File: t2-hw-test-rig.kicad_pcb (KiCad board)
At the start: 2 copper layers, 86.4 x 94 mm, 152 parts, among them J101 CONN_01X02, J102 BARREL_JACK, J103 CONN_01X02, J201 MICROUSB-TH, J202 CONN_01X02, J203 MICROUSB-TH, J204 USB_A_TH, J301 CONN_02x05, 0.05", Q101 pMOS, Q401 CJ2302, Q402 CJ2302, Q403 CJ2302, Q404 CJ2302, Q405 CJ2302 DNP, Q406 CJ2302 DNP, SW301 Switch_DPST, SW302 Switch_DPST, U101 MAX6102, U102 XC6206P332MR-G, U301 ATSAMD21J18A-MUT, U302 AAT4610, U303 AAT4610, U401 MAX9919FASA+, U402 MAX9919FASA+, U403 MAX9919FASA+, U404 MAX9919FASA+, U405 MAX9919FASA+, U501 TSV324IDT, U502 TSV324IDT, U503 TSV324IDT, X301 FC-135

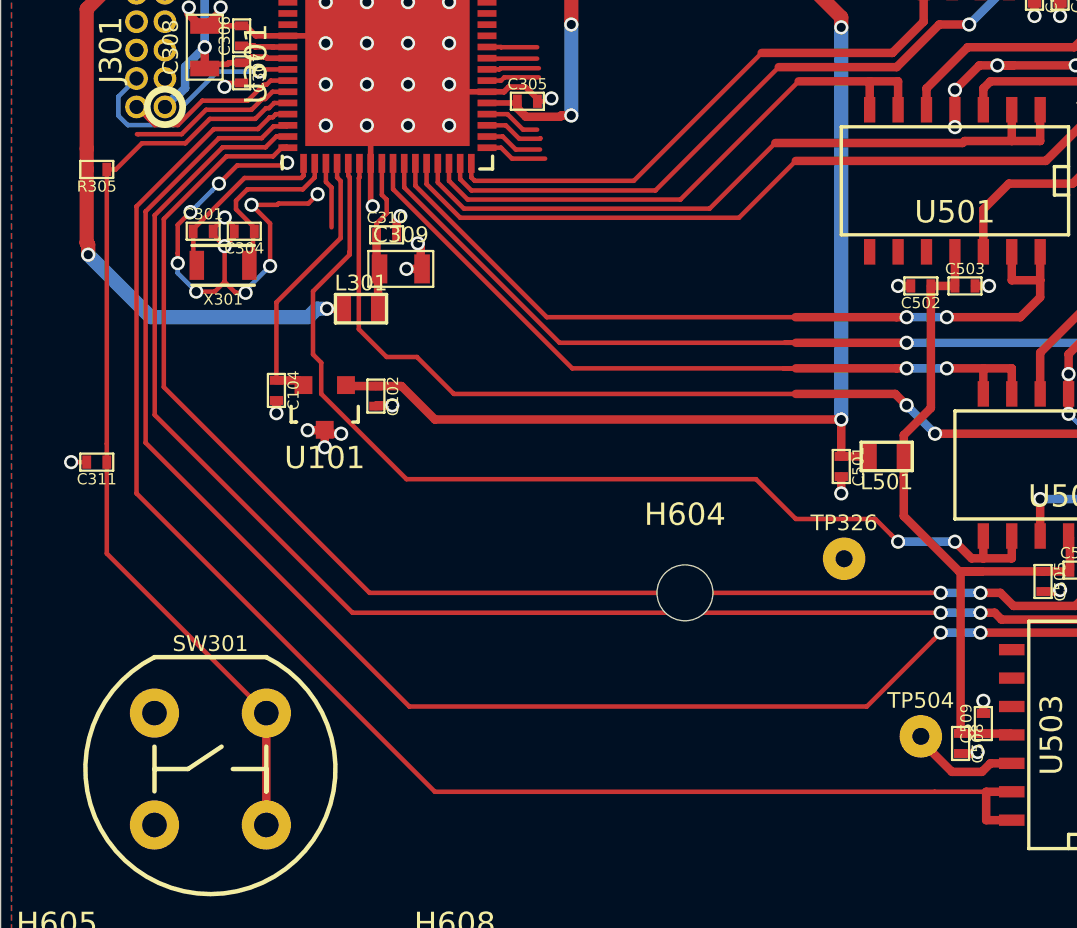
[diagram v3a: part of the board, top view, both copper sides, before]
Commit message: now with fewer traces through mounting holes...
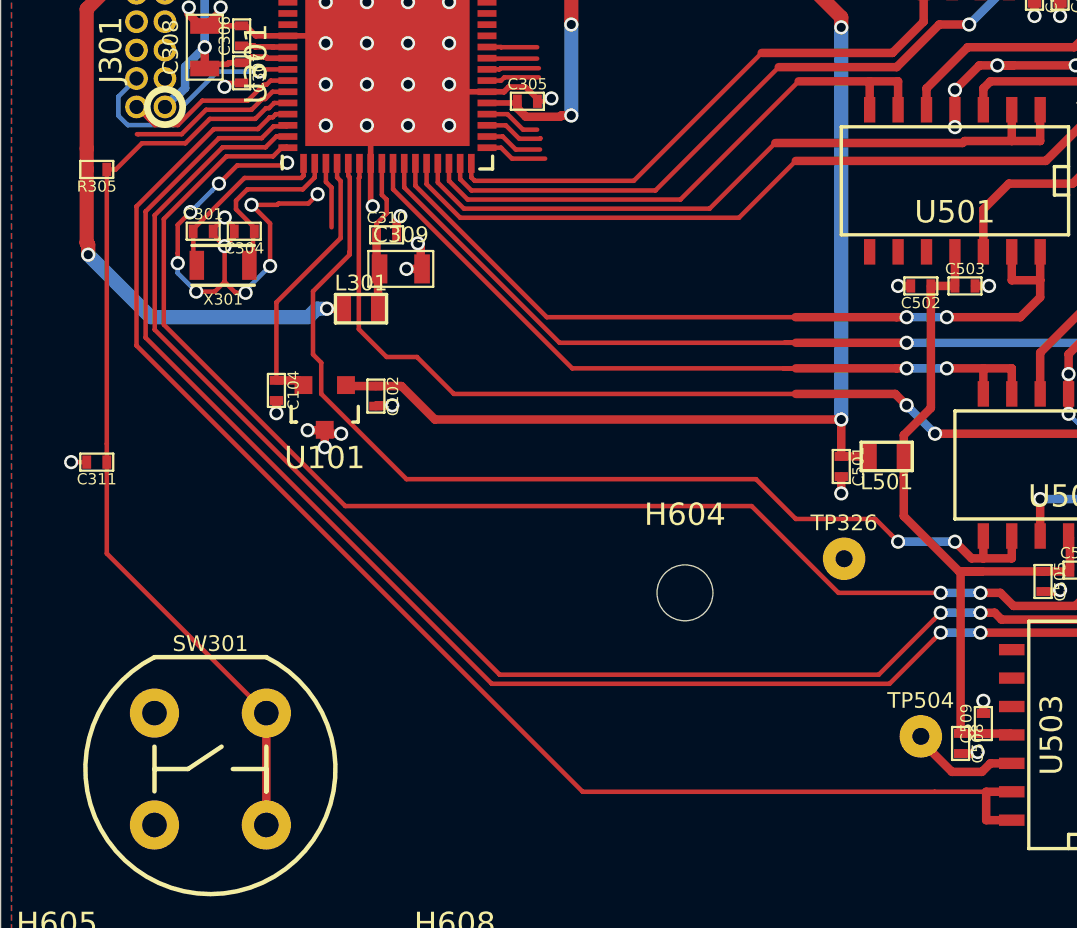
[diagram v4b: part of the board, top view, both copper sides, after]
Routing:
- net 18_BUFF: track 68.4 -> 64.5 mm
- net 33MT_DIV_BUFF: track 74.7 -> 71.1 mm
- net 5VUSB0_DIV_BUFF: track 67.7 -> 66.0 mm
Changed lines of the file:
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@@
     (thickness 1.6)
     (drawings 1404)
-    (tracks 1513)
+    (tracks 1516)
     (zones 0)
     (modules 152)
@@
   )
   (setup
-    (last_trace_width 0.381)
+    (last_trace_width 0.2032)
     (user_trace_width 0.254)
     (user_trace_width 0.381)
@@
   (segment (start 110.887231 113.678036) (end 104.169267 120.396) (width 0.381) (layer F.Cu) (net 63))
   (segment (start 104.169267 120.396) (end 104.139998 120.396) (width 0.381) (layer F.Cu) (net 63))
-  (segment (start 62.663334 111.65841) (end 63.143491 111.178253) (width 0.2032) (layer F.Cu) (net 64))
-  (segment (start 66.548 132.461) (end 57.70882 123.62182) (width 0.2032) (layer F.Cu) (net 64))
-  (segment (start 63.143491 111.178253) (end 63.659753 111.178253) (width 0.2032) (layer F.Cu) (net 64))
-  (segment (start 57.70882 114.69693) (end 60.74734 111.65841) (width 0.2032) (layer F.Cu) (net 64))
-  (segment (start 60.74734 111.65841) (end 62.663334 111.65841) (width 0.2032) (layer F.Cu) (net 64))
-  (segment (start 92.837 132.461) (end 66.548 132.461) (width 0.2032) (layer F.Cu) (net 64))
-  (segment (start 57.70882 123.62182) (end 57.70882 114.69693) (width 0.2032) (layer F.Cu) (net 64))
+  (segment (start 92.519501 132.778499) (end 92.837 132.461) (width 0.2032) (layer F.Cu) (net 64))
+  (segment (start 90.06841 135.22959) (end 92.519501 132.778499) (width 0.2032) (layer F.Cu) (net 64))
+  (segment (start 73.12659 135.22959) (end 90.06841 135.22959) (width 0.2032) (layer F.Cu) (net 64))
+  (segment (start 62.663334 111.65841) (end 60.74734 111.65841) (width 0.2032) (layer F.Cu) (net 64))
+  (segment (start 60.74734 111.65841) (end 57.70882 114.69693) (width 0.2032) (layer F.Cu) (net 64))
+  (segment (start 57.70882 114.69693) (end 57.70882 119.81182) (width 0.2032) (layer F.Cu) (net 64))
+  (segment (start 63.143491 111.178253) (end 62.663334 111.65841) (width 0.2032) (layer F.Cu) (net 64))
+  (segment (start 63.659753 111.178253) (end 63.143491 111.178253) (width 0.2032) (layer F.Cu) (net 64))
+  (segment (start 57.70882 119.81182) (end 73.12659 135.22959) (width 0.2032) (layer F.Cu) (net 64))
   (segment (start 94.615 132.461) (end 92.837 132.461) (width 0.381) (layer B.Cu) (net 64))
   (via (at 92.837 132.461) (size 0.635) (drill 0.4064) (layers F.Cu B.Cu) (net 64))
@@
   (segment (start 103.378 123.698) (end 102.616 124.46) (width 0.381) (layer F.Cu) (net 68))
   (via (at 91.313 123.19) (size 0.635) (drill 0.4064) (layers F.Cu B.Cu) (net 68))
-  (segment (start 92.387988 131.572) (end 92.837 131.572) (width 0.2032) (layer F.Cu) (net 69))
-  (segment (start 58.11523 114.86527) (end 58.11523 122.37723) (width 0.2032) (layer F.Cu) (net 69))
-  (segment (start 60.91568 112.06482) (end 58.11523 114.86527) (width 0.2032) (layer F.Cu) (net 69))
   (segment (start 63.659753 111.678253) (end 63.384753 111.678253) (width 0.2032) (layer F.Cu) (net 69))
-  (segment (start 67.31 131.572) (end 92.387988 131.572) (width 0.2032) (layer F.Cu) (net 69))
-  (segment (start 62.998186 112.06482) (end 60.91568 112.06482) (width 0.2032) (layer F.Cu) (net 69))
-  (segment (start 58.11523 122.37723) (end 67.31 131.572) (width 0.2032) (layer F.Cu) (net 69))
+  (segment (start 58.11523 114.86527) (end 58.11523 119.58323) (width 0.2032) (layer F.Cu) (net 69))
   (segment (start 63.384753 111.678253) (end 62.998186 112.06482) (width 0.2032) (layer F.Cu) (net 69))
+  (segment (start 62.998186 112.06482) (end 60.91568 112.06482) (width 0.2032) (layer F.Cu) (net 69))
+  (segment (start 88.265 131.572) (end 92.837 131.572) (width 0.2032) (layer F.Cu) (net 69))
+  (segment (start 60.91568 112.06482) (end 58.11523 114.86527) (width 0.2032) (layer F.Cu) (net 69))
+  (segment (start 58.11523 119.58323) (end 66.225923 127.693923) (width 0.2032) (layer F.Cu) (net 69))
+  (segment (start 66.225923 127.693923) (end 84.386923 127.693923) (width 0.2032) (layer F.Cu) (net 69))
+  (segment (start 84.386923 127.693923) (end 88.265 131.572) (width 0.2032) (layer F.Cu) (net 69))
   (segment (start 94.615 131.572) (end 92.837 131.572) (width 0.381) (layer B.Cu) (net 69))
   (segment (start 63.659753 111.678253) (end 63.614554 111.633054) (width 0.2032) (layer F.Cu) (net 69))
@@
   (via (at 90.932 129.286) (size 0.635) (drill 0.4064) (layers F.Cu B.Cu) (net 70))
   (segment (start 60.579 111.252) (end 57.30241 114.52859) (width 0.2032) (layer F.Cu) (net 71))
-  (segment (start 89.535 136.652) (end 92.519501 133.667499) (width 0.2032) (layer F.Cu) (net 71))
-  (segment (start 57.30241 114.52859) (end 57.30241 124.86641) (width 0.2032) (layer F.Cu) (net 71))
-  (segment (start 69.088 136.652) (end 89.535 136.652) (width 0.2032) (layer F.Cu) (net 71))
+  (segment (start 90.551 135.636) (end 92.519501 133.667499) (width 0.2032) (layer F.Cu) (net 71))
   (segment (start 62.4905 111.252) (end 60.579 111.252) (width 0.2032) (layer F.Cu) (net 71))
-  (segment (start 92.519501 133.667499) (end 92.837 133.35) (width 0.2032) (layer F.Cu) (net 71))
+  (segment (start 63.019048 110.723452) (end 62.4905 111.252) (width 0.2032) (layer F.Cu) (net 71))
+  (segment (start 57.30241 114.52859) (end 57.30241 120.16741) (width 0.2032) (layer F.Cu) (net 71))
   (segment (start 63.659753 110.678253) (end 63.614554 110.723452) (width 0.2032) (layer F.Cu) (net 71))
   (segment (start 63.614554 110.723452) (end 63.019048 110.723452) (width 0.2032) (layer F.Cu) (net 71))
-  (segment (start 57.30241 124.86641) (end 69.088 136.652) (width 0.2032) (layer F.Cu) (net 71))
-  (segment (start 63.019048 110.723452) (end 62.4905 111.252) (width 0.2032) (layer F.Cu) (net 71))
+  (segment (start 57.30241 120.16741) (end 72.771 135.636) (width 0.2032) (layer F.Cu) (net 71))
+  (segment (start 72.771 135.636) (end 90.551 135.636) (width 0.2032) (layer F.Cu) (net 71))
+  (segment (start 92.519501 133.667499) (end 92.837 133.35) (width 0.2032) (layer F.Cu) (net 71))
   (segment (start 94.615 133.35) (end 92.837 133.35) (width 0.381) (layer B.Cu) (net 71))
   (segment (start 103.505 134.112) (end 102.362 134.112) (width 0.381) (layer F.Cu) (net 71))
@@
   (segment (start 56.970209 111.074211) (end 56.912265 111.074211) (width 0.2032) (layer F.Cu) (net 91))
   (segment (start 63.659753 110.178253) (end 63.122997 110.178253) (width 0.2032) (layer F.Cu) (net 92))
-  (segment (start 70.231 140.462) (end 92.567394 140.462) (width 0.2032) (layer F.Cu) (net 92))
   (segment (start 63.122997 110.178253) (end 62.984206 110.317044) (width 0.2032) (layer F.Cu) (net 92))
+  (segment (start 62.32216 110.84559) (end 60.35041 110.84559) (width 0.2032) (layer F.Cu) (net 92))
   (segment (start 62.984206 110.317044) (end 62.850706 110.317044) (width 0.2032) (layer F.Cu) (net 92))
   (segment (start 62.850706 110.317044) (end 62.32216 110.84559) (width 0.2032) (layer F.Cu) (net 92))
-  (segment (start 62.32216 110.84559) (end 60.35041 110.84559) (width 0.2032) (layer F.Cu) (net 92))
   (segment (start 60.35041 110.84559) (end 56.896 114.3) (width 0.2032) (layer F.Cu) (net 92))
-  (segment (start 56.896 114.3) (end 56.896 127.127) (width 0.2032) (layer F.Cu) (net 92))
-  (segment (start 56.896 127.127) (end 70.231 140.462) (width 0.2032) (layer F.Cu) (net 92))
   (segment (start 92.567394 140.462) (end 94.869 140.462) (width 0.2032) (layer F.Cu) (net 92))
+  (segment (start 56.896 114.3) (end 56.896 120.523) (width 0.2032) (layer F.Cu) (net 92))
+  (segment (start 56.896 120.523) (end 76.835 140.462) (width 0.2032) (layer F.Cu) (net 92))
+  (segment (start 76.835 140.462) (end 92.567394 140.462) (width 0.2032) (layer F.Cu) (net 92))
   (segment (start 94.869 141.732) (end 96.012 141.732) (width 0.381) (layer F.Cu) (net 92))
   (segment (start 94.869 140.462) (end 94.869 141.732) (width 0.381) (layer F.Cu) (net 92))

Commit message: time to move on to the digital side
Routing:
- net /OP AMPS/UUT_12: track 8.74 -> 8.22 mm
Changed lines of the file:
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@@
   (segment (start 110.887231 113.678036) (end 104.169267 120.396) (width 0.381) (layer F.Cu) (net 63))
   (segment (start 104.169267 120.396) (end 104.139998 120.396) (width 0.381) (layer F.Cu) (net 63))
-  (segment (start 92.519501 132.778499) (end 92.837 132.461) (width 0.2032) (layer F.Cu) (net 64))
-  (segment (start 90.06841 135.22959) (end 92.519501 132.778499) (width 0.2032) (layer F.Cu) (net 64))
-  (segment (start 73.12659 135.22959) (end 90.06841 135.22959) (width 0.2032) (layer F.Cu) (net 64))
+  (segment (start 63.659753 111.178253) (end 63.143491 111.178253) (width 0.2032) (layer F.Cu) (net 64))
+  (segment (start 63.143491 111.178253) (end 62.663334 111.65841) (width 0.2032) (layer F.Cu) (net 64))
   (segment (start 62.663334 111.65841) (end 60.74734 111.65841) (width 0.2032) (layer F.Cu) (net 64))
+  (segment (start 73.025 135.128) (end 90.17 135.128) (width 0.2032) (layer F.Cu) (net 64))
   (segment (start 60.74734 111.65841) (end 57.70882 114.69693) (width 0.2032) (layer F.Cu) (net 64))
   (segment (start 57.70882 114.69693) (end 57.70882 119.81182) (width 0.2032) (layer F.Cu) (net 64))
-  (segment (start 63.143491 111.178253) (end 62.663334 111.65841) (width 0.2032) (layer F.Cu) (net 64))
-  (segment (start 63.659753 111.178253) (end 63.143491 111.178253) (width 0.2032) (layer F.Cu) (net 64))
-  (segment (start 57.70882 119.81182) (end 73.12659 135.22959) (width 0.2032) (layer F.Cu) (net 64))
+  (segment (start 57.70882 119.81182) (end 73.025 135.128) (width 0.2032) (layer F.Cu) (net 64))
+  (segment (start 90.17 135.128) (end 92.519501 132.778499) (width 0.2032) (layer F.Cu) (net 64))
+  (segment (start 92.519501 132.778499) (end 92.837 132.461) (width 0.2032) (layer F.Cu) (net 64))
   (segment (start 94.615 132.461) (end 92.837 132.461) (width 0.381) (layer B.Cu) (net 64))
   (via (at 92.837 132.461) (size 0.635) (drill 0.4064) (layers F.Cu B.Cu) (net 64))
@@
   (via (at 91.313 123.19) (size 0.635) (drill 0.4064) (layers F.Cu B.Cu) (net 68))
   (segment (start 63.659753 111.678253) (end 63.384753 111.678253) (width 0.2032) (layer F.Cu) (net 69))
-  (segment (start 58.11523 114.86527) (end 58.11523 119.58323) (width 0.2032) (layer F.Cu) (net 69))
   (segment (start 63.384753 111.678253) (end 62.998186 112.06482) (width 0.2032) (layer F.Cu) (net 69))
+  (segment (start 60.91568 112.06482) (end 58.11523 114.86527) (width 0.2032) (layer F.Cu) (net 69))
+  (segment (start 88.265 131.572) (end 92.837 131.572) (width 0.2032) (layer F.Cu) (net 69))
   (segment (start 62.998186 112.06482) (end 60.91568 112.06482) (width 0.2032) (layer F.Cu) (net 69))
-  (segment (start 88.265 131.572) (end 92.837 131.572) (width 0.2032) (layer F.Cu) (net 69))
-  (segment (start 60.91568 112.06482) (end 58.11523 114.86527) (width 0.2032) (layer F.Cu) (net 69))
-  (segment (start 58.11523 119.58323) (end 66.225923 127.693923) (width 0.2032) (layer F.Cu) (net 69))
-  (segment (start 66.225923 127.693923) (end 84.386923 127.693923) (width 0.2032) (layer F.Cu) (net 69))
+  (segment (start 66.352923 127.693923) (end 84.386923 127.693923) (width 0.2032) (layer F.Cu) (net 69))
+  (segment (start 58.11523 114.86527) (end 58.11523 119.45623) (width 0.2032) (layer F.Cu) (net 69))
+  (segment (start 58.11523 119.45623) (end 66.352923 127.693923) (width 0.2032) (layer F.Cu) (net 69))
   (segment (start 84.386923 127.693923) (end 88.265 131.572) (width 0.2032) (layer F.Cu) (net 69))
   (segment (start 94.615 131.572) (end 92.837 131.572) (width 0.381) (layer B.Cu) (net 69))
@@
   (segment (start 129.54 102.87) (end 127.454502 102.87) (width 0.381) (layer F.Cu) (net 96))
   (segment (start 127.454502 102.87) (end 126.111 102.87) (width 0.381) (layer F.Cu) (net 96))
-  (segment (start 98.7298 113.284) (end 100.4062 111.6076) (width 0.381) (layer F.Cu) (net 97))
-  (segment (start 95.885 113.284) (end 98.7298 113.284) (width 0.381) (layer F.Cu) (net 97))
-  (segment (start 94.742 114.427) (end 95.885 113.284) (width 0.381) (layer F.Cu) (net 97))
-  (segment (start 94.742 116.332) (end 94.742 114.427) (width 0.381) (layer F.Cu) (net 97))
+  (segment (start 94.742 116.332) (end 94.742 115.316) (width 0.381) (layer F.Cu) (net 97))
+  (segment (start 94.742 115.316) (end 95.885 114.173) (width 0.381) (layer F.Cu) (net 97))
+  (segment (start 97.8408 114.173) (end 100.4062 111.6076) (width 0.381) (layer F.Cu) (net 97))
+  (segment (start 95.885 114.173) (end 97.8408 114.173) (width 0.381) (layer F.Cu) (net 97))
   (segment (start 91.948 138.182352) (end 91.948 137.9855) (width 0.381) (layer F.Cu) (net 98))
   (segment (start 93.338648 139.573) (end 91.948 138.182352) (width 0.381) (layer F.Cu) (net 98))

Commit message: port b
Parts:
- moved R406 3.43 mm to (89.8, 97.8)
- moved R401 0.54 mm to (115.7, 104.8), turned to 90 degrees
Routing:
- net /SAM/PORT_B_G3: track 2.96 -> 66.1 mm, vias 0 -> 5
- net USB1_SHORT: track 7.33 -> 63.8 mm, vias 0 -> 4
- net PA33_SHORT: track 4.02 -> 59.0 mm, vias 0 -> 2
- net /SAM/UUT_~RESET: track 0.00 -> 53.1 mm, vias 0 -> 2
- net USB0_SHORT: track 8.27 -> 60.5 mm, vias 0 -> 4
- net /SAM/UUT_SWCLK: track 2.34 -> 42.0 mm, vias 0 -> 5
- net /SAM/UUT_SWDIO: track 2.38 -> 37.6 mm, vias 0 -> 5
- net /SAM/PORT_B_SCL: track 2.25 -> 29.5 mm, vias 0 -> 2
- net PB33_SHORT: track 3.74 -> 29.0 mm, vias 0 -> 2
- net /SAM/PORT_B_SCK: track 0.00 -> 25.2 mm, vias 0 -> 2
- net /SAM/PORT_B_SDA: track 2.25 -> 27.4 mm, vias 0 -> 2
- net /SAM/PORT_B_MISO: track 0.00 -> 23.9 mm, vias 0 -> 2
- net /SAM/PORT_B_MOSI: track 0.00 -> 21.7 mm, vias 0 -> 2
- net +5V: track 193.9 -> 174.4 mm
- net /SAM/PORT_B_G1/TX: track 0.00 -> 19.5 mm, vias 0 -> 2
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
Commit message: routed
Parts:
- moved C103 24.5 mm to (74.4, 97.2), turned to 90 degrees
- moved U102 22.1 mm to (72.3, 97.7), turned to 270 degrees
- moved C105 21.8 mm to (71.5, 99.8), turned to 0 degrees
- moved R310 21.6 mm to (56.9, 102.4), turned to 180 degrees
- moved C314 19.2 mm to (56.9, 101.1), turned to 180 degrees
- moved C303 0.97 mm to (72.4, 102.2), turned to 0 degrees
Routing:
- net /SAM/PORT_A_MOSI: track 7.53 -> 169.0 mm, vias 0 -> 6
- net /SAM/FAIL_LED: track 0.00 -> 136.3 mm, vias 0 -> 2
- net /SAM/PASS_LED: track 0.00 -> 134.0 mm, vias 0 -> 2
- net GND: track 444.3 -> 570.4 mm, vias 185 -> 212
- net /SAM/READY_LED: track 0.00 -> 117.8 mm, vias 0 -> 2
- net /SAM/TEST_IN_PROGRESS_LED: track 0.00 -> 108.4 mm, vias 0 -> 4
- net /SAM/UUT_~ENABLE~_USB: track 1.27 -> 107.4 mm, vias 0 -> 10
- net /SAM/UUT_~ENABLE~_VIN: track 1.41 -> 106.7 mm, vias 0 -> 8
- net /SAM/PORT_A_SCK: track 0.00 -> 88.3 mm, vias 0 -> 4
- net /SAM/PORT_A_SCL: track 0.00 -> 86.6 mm, vias 0 -> 2
- net /SAM/PORT_A_MISO: track 0.00 -> 84.4 mm, vias 0 -> 4
- net /SAM/PORT_A_G1/TX: track 0.00 -> 71.3 mm, vias 0 -> 2
- net /SAM/PORT_A_G2/RX: track 0.00 -> 70.2 mm, vias 0 -> 2
- net /SAM/PORT_A_G3: track 0.00 -> 68.0 mm, vias 0 -> 2
- net /SAM/PORT_A_SDA: track 0.00 -> 65.8 mm, vias 0 -> 4
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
